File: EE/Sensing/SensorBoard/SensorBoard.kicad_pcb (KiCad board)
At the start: 2 copper layers, 113 parts, among them J1 Conn_02x13_Odd_Even, J101 Peg, J102 Peg, J11 Peg, J12 Peg, J21 Peg, J22 Peg, J31 Peg, J32 Peg, J41 Peg, J42 Peg, J51 Peg, J52 Peg, J61 Peg, J62 Peg, J71 Peg, J72 Peg, J81 Peg, J82 Peg, J91 Peg, J92 Peg, Q1 BSS84DW, Q10 BSS84DW, Q2 BSS84DW, Q3 BSS84DW, Q4 BSS84DW, Q5 BSS84DW, Q6 BSS84DW, Q7 BSS84DW, Q8 BSS84DW, Q9 BSS84DW, U1 TCR2EE27, U101 AH1381, U102 AH1381, U11 AH1381, U12 AH1381, U2 TCR2EE32, U21 AH1381, U22 AH1381, U31 AH1381, U32 AH1381, U41 AH1381, U42 AH1381, U51 AH1381, U52 AH1381, U61 AH1381, U62 AH1381, U71 AH1381, U72 AH1381, U81 AH1381, U82 AH1381, U91 AH1381, U92 AH1381

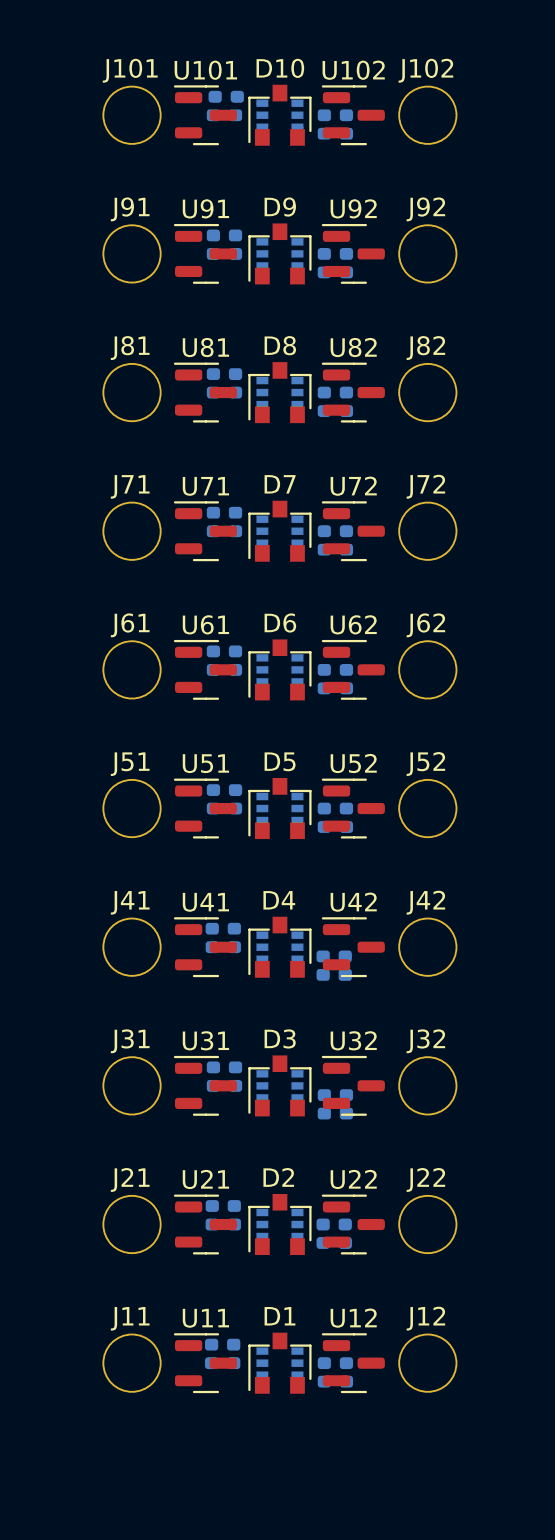
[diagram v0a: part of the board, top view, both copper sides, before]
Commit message: All on top layer
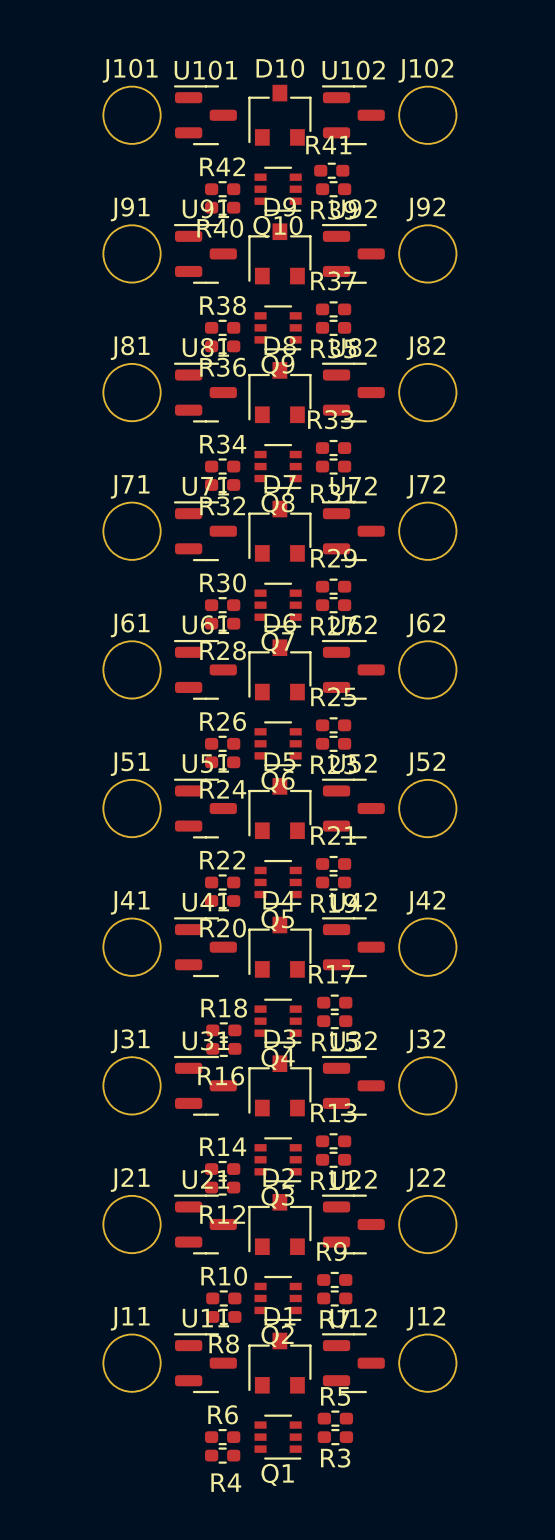
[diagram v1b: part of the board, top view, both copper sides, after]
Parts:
- Q1, Q10, Q2, Q3, Q4, Q5, Q6, Q7, Q8, Q9, R10, R11, R12, R13, R14, R15, R16, R17, R18, R19, R20, R21, R22, R23, R24, R25, R26, R27, R28, R29, R3, R30, R31, R32, R33, R34, R35, R36, R37, R38, R39, R4, R40, R41, R42, R5, R6, R7, R8, R9: moved to F.Cu
- moved R12 7.29 mm to (226.0, 80.5), turned to 0 degrees
- moved R14 7.29 mm to (226.0, 79.5), turned to 0 degrees
- moved R20 7.29 mm to (226.0, 65.0), turned to 0 degrees
- moved R22 7.29 mm to (226.0, 64.0), turned to 0 degrees
- moved R24 7.29 mm to (226.0, 57.5), turned to 0 degrees
- moved R26 7.29 mm to (226.0, 56.5), turned to 0 degrees
- moved R28 7.29 mm to (226.0, 50.0), turned to 0 degrees
- moved R3 7.29 mm to (232.1, 94.0), turned to 180 degrees
- moved R30 7.29 mm to (226.0, 49.0), turned to 0 degrees
- moved R32 7.29 mm to (226.0, 42.5), turned to 180 degrees
- moved R34 7.29 mm to (226.0, 41.5), turned to 0 degrees
- moved R36 7.29 mm to (226.0, 35.0), turned to 180 degrees
- moved R38 7.29 mm to (226.0, 34.0), turned to 0 degrees
- moved R4 7.29 mm to (226.0, 95.0), turned to 0 degrees
- moved R40 7.29 mm to (226.0, 27.5), turned to 0 degrees
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
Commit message: Front Layout, Smaller silkscreen
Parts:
- moved C1 61.6 mm to (257.2, 25.7)
- moved C3 61.6 mm to (259.4, 26.5)
- moved R1 61.6 mm to (256.2, 23.2)
- moved U1 61.6 mm to (258.7, 24.0)
- moved C2 61.6 mm to (265.1, 26.0)
- moved C4 61.6 mm to (267.4, 26.7)
- moved R2 61.6 mm to (264.1, 23.5)
- moved U2 61.6 mm to (266.6, 24.2)
- moved H2 57.8 mm to (215.5, 41.5)
- moved H1 55.1 mm to (216.5, 69.0)
- moved R12 6.95 mm to (232.0, 77.0), turned to 180 degrees
- moved R16 6.84 mm to (231.9, 69.5), turned to 180 degrees
- moved R20 6.53 mm to (232.0, 62.5), turned to 180 degrees
- moved R32 6.53 mm to (232.0, 40.0), turned to 0 degrees
- moved R36 6.53 mm to (232.0, 32.5), turned to 0 degrees
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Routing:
- net /2v7: track 2.91 -> 24.8 mm
- net /B1_0_4: track 0.00 -> 17.9 mm, vias 0 -> 2
- net /B1_1_4: track 0.00 -> 13.5 mm
- net Net-(D10-Pad1): track 0.00 -> 6.30 mm, vias 0 -> 2
- net GND: track 8.34 -> 13.6 mm, vias 8 -> 11
- net Net-(D10-Pad2): track 0.00 -> 3.33 mm
- net Net-(Q10-Pad3): track 0.20 -> 1.70 mm
- net Net-(Q10-Pad6): track 0.20 -> 1.51 mm

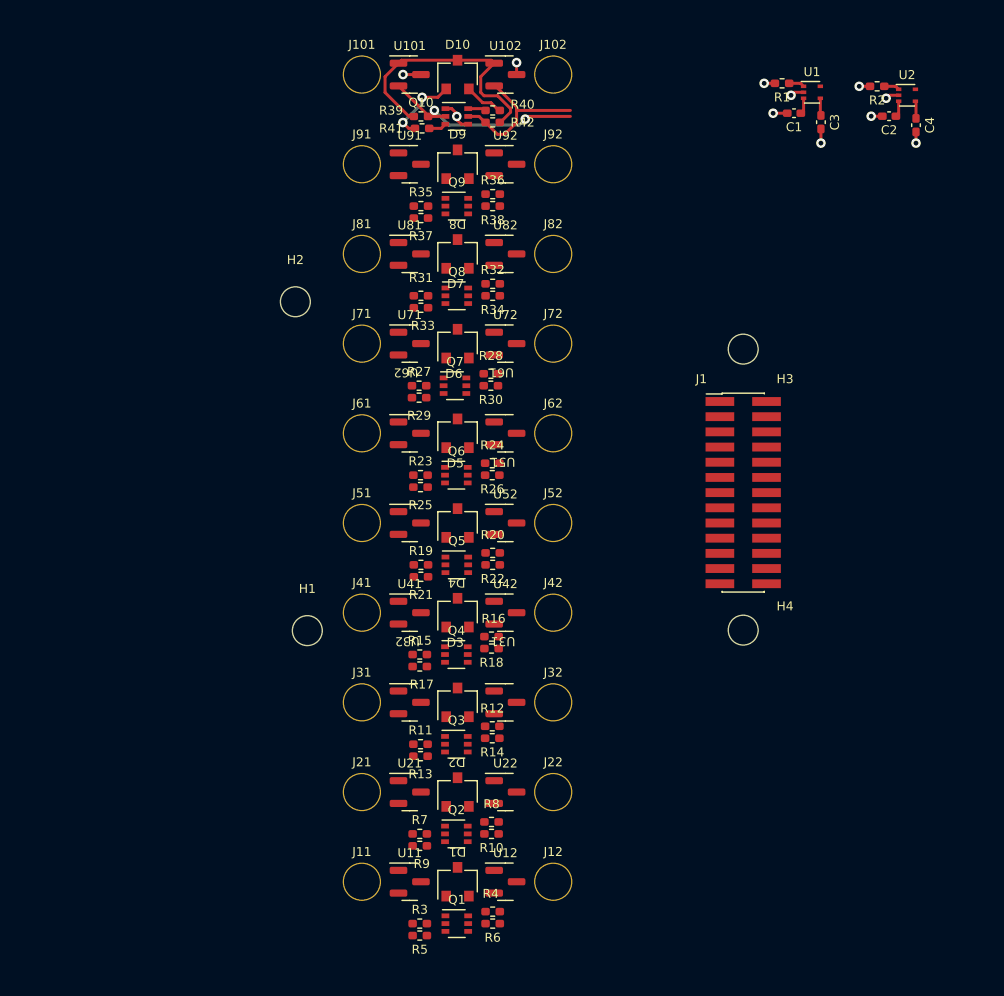
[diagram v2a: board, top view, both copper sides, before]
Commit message: Sensors attached to mainboard
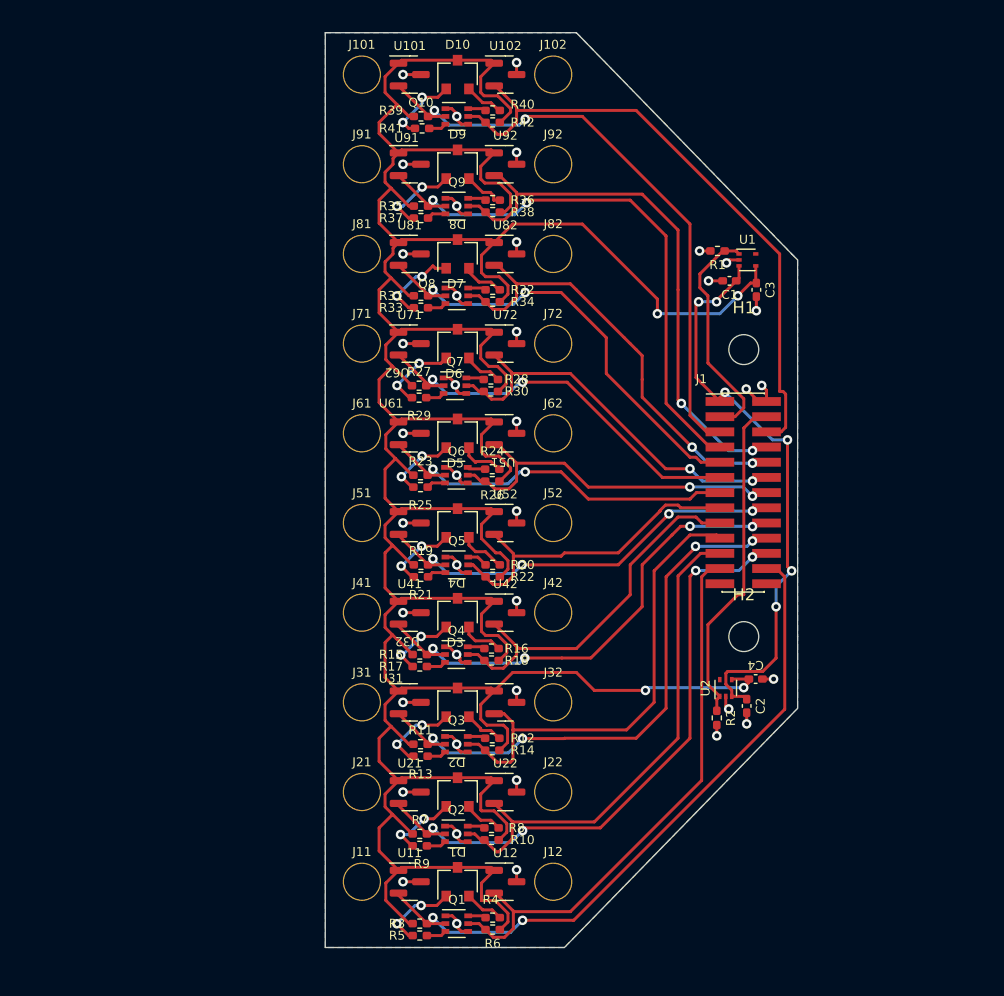
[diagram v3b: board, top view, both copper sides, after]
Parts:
- removed H3, H4: MountingHole, MountingHole:MountingHole_2.5mm
- moved R2 54.5 mm to (250.7, 76.3), turned to -90 degrees
- moved U2 51.8 mm to (251.5, 73.8), turned to 90 degrees
- moved C2 50.7 mm to (253.2, 75.3), turned to -90 degrees
- moved C4 48.2 mm to (254.0, 73.0), turned to 0 degrees
- moved H2 46.8 mm to (253.0, 69.5)
- moved H1 43.4 mm to (253.0, 45.5)
- moved C1 15.0 mm to (251.8, 39.8)
- moved C3 15.0 mm to (254.1, 40.5)
- moved R1 15.0 mm to (250.8, 37.2)
- moved U1 15.0 mm to (253.3, 38.0)
- moved R12 1.00 mm to (232.0, 78.0)
- moved R14 1.00 mm to (232.0, 79.0)
- moved R16 1.00 mm to (231.9, 70.5)
- moved R18 1.00 mm to (231.9, 71.5)
- moved R20 1.00 mm to (232.0, 63.5)
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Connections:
- J1 pad 10: /B0_0_2 -> /B1_1_2
- J1 pad 11: /B0_1_1 -> /B1_0_1
- J1 pad 12: /B0_0_1 -> /B1_1_1
- J1 pad 13: /B0_1_0 -> /B1_0_0
- J1 pad 14: /B0_0_0 -> /B1_1_0
- J1 pad 15: /B1_1_4 -> /B0_1_4
- J1 pad 16: /B1_0_4 -> /B0_0_4
- J1 pad 17: /B1_1_3 -> /B0_1_3
- J1 pad 18: /B1_0_3 -> /B0_0_3
- J1 pad 19: /B1_1_2 -> /B0_1_2
- J1 pad 20: /B1_0_2 -> /B0_0_2
- J1 pad 21: /B1_1_1 -> /B0_1_1
- J1 pad 22: /B1_1_0 -> /B0_0_1
- J1 pad 23: /B1_0_1 -> /B0_1_0
- J1 pad 24: /B1_0_0 -> /B0_0_0
- J1 pad 5: /B0_1_4 -> /B1_0_4
- J1 pad 6: /B0_0_4 -> /B1_1_4
- J1 pad 7: /B0_1_3 -> /B1_0_3
- J1 pad 8: /B0_0_3 -> /B1_1_3
- J1 pad 9: /B0_1_2 -> /B1_0_2
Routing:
- net /2v7: track 24.8 -> 319.2 mm, vias 0 -> 4
- net /B0_0_0: track 0.00 -> 56.3 mm, vias 0 -> 2
- net /B0_0_1: track 0.00 -> 52.1 mm, vias 0 -> 4
- net GND: track 13.6 -> 65.3 mm, vias 11 -> 40
- net /B0_0_2: track 0.00 -> 48.1 mm, vias 0 -> 4
- net /B1_0_3: track 0.00 -> 47.5 mm, vias 0 -> 2
- net /B0_1_0: track 0.00 -> 47.4 mm
- net VCC: track 2.69 -> 49.6 mm, vias 0 -> 6
- net /B1_1_3: track 0.00 -> 46.9 mm, vias 0 -> 2
- net /B0_1_1: track 0.00 -> 43.2 mm
- net /B0_0_3: track 0.00 -> 41.1 mm, vias 0 -> 4
- net /B0_1_2: track 0.00 -> 40.1 mm
- net /B1_1_4: track 13.5 -> 52.6 mm
- net /B1_0_2: track 0.00 -> 38.3 mm, vias 0 -> 2
- net /B1_1_2: track 0.00 -> 37.8 mm, vias 0 -> 2
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- added copper zone on B.Cu, net GND
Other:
- board outline added: 39.5 x 76.5 mm
